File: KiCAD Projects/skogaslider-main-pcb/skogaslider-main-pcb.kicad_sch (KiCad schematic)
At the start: 173 parts, among them J1 USB_C_Receptacle_USB2.0, J2 USB_C_Receptacle_USB2.0, J4 Conn_02x16_Top_Bottom, J5 USB_C_Receptacle_USB2.0, J6 USB_C_Receptacle_USB2.0, Q1 BSS138, U1 NCP1117-3.3_SOT223, U2 MPR121QR2, U3 MPR121QR2, U4 USBLC6-2P6, U5 RP2040, U6 M24C02-RMN, U7 W25Q128JVS, U8 MPR121QR2, Y1 ABLS-12.000MHZ-B4-T

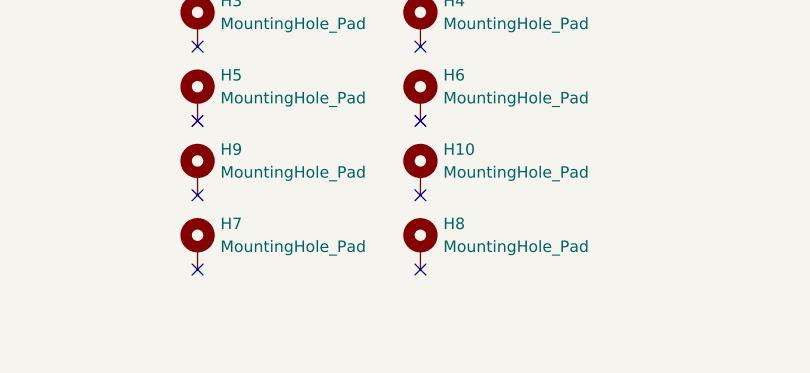
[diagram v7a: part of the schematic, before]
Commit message: Minor revision of the slider PCB to re-arrange the mounting holes to fit the CAD better.
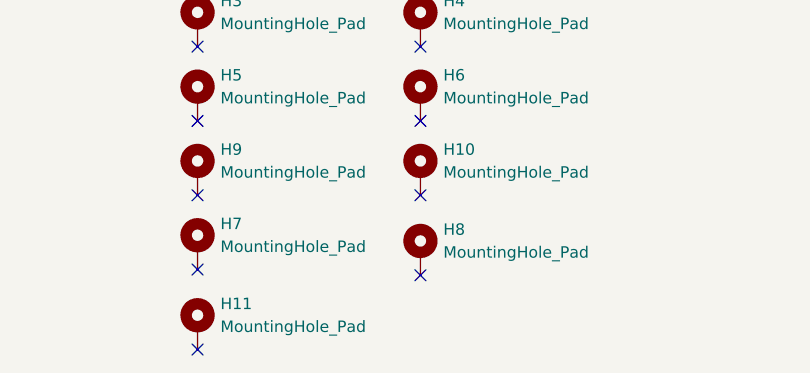
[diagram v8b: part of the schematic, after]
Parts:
- added H11: MountingHole_Pad, MountingHole:MountingHole_3.2mm_M3_DIN965_Pad_TopBottom, symbol Mechanical:MountingHole_Pad
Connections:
- no-connect marks 53 -> 54
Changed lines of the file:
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@@
   (no_connect (at 287.02 128.905))
   (no_connect (at 287.02 131.445))
-  (no_connect (at 133.985 341.63))
+  (no_connect (at 109.22 350.52))
   (no_connect (at 487.045 63.5))
   (no_connect (at 133.985 308.61))
@@
   (no_connect (at 287.02 106.045))
   (no_connect (at 134.62 56.515))
+  (no_connect (at 133.985 342.265))
   (no_connect (at 109.22 308.61))
   (no_connect (at 287.02 108.585))
@@
     (pin "D1")
   )
-  (symbol (lib_id "Mechanical:MountingHole_Pad") (at 133.985 339.09 0) (unit 1)
-    (in_bom yes) (on_board yes) (fields_autoplaced)
-    (property "Reference" "H8" (id 0) (at 136.525 336.5499 0)
-      (effects (font (size 1.27 1.27)) (justify left))
-    )
-    (property "Value" "MountingHole_Pad" (id 1) (at 136.525 339.0899 0)
-      (effects (font (size 1.27 1.27)) (justify left))
-    )
-    (property "Footprint" "MountingHole:MountingHole_3.2mm_M3_DIN965_Pad_TopBottom" (id 2) (at 133.985 339.09 0)
-      (effects (font (size 1.27 1.27)) hide)
-    )
-    (property "Datasheet" "~" (id 3) (at 133.985 339.09 0)
-      (effects (font (size 1.27 1.27)) hide)
-    )
-    (pin "1")
-  )
   (symbol (lib_id "Device:C") (at 454.66 213.36 0) (unit 1)
     (in_bom yes) (on_board yes)
@@
     (pin "2")
   )
+  (symbol (lib_id "Mechanical:MountingHole_Pad") (at 133.985 339.725 0) (unit 1)
+    (in_bom yes) (on_board yes) (fields_autoplaced)
+    (property "Reference" "H8" (id 0) (at 136.525 337.1849 0)
+      (effects (font (size 1.27 1.27)) (justify left))
+    )
+    (property "Value" "MountingHole_Pad" (id 1) (at 136.525 339.7249 0)
+      (effects (font (size 1.27 1.27)) (justify left))
+    )
+    (property "Footprint" "MountingHole:MountingHole_3.2mm_M3_DIN965_Pad_TopBottom" (id 2) (at 133.985 339.725 0)
+      (effects (font (size 1.27 1.27)) hide)
+    )
+    (property "Datasheet" "~" (id 3) (at 133.985 339.725 0)
+      (effects (font (size 1.27 1.27)) hide)
+    )
+    (pin "1")
+  )
   (symbol (lib_id "power:GND") (at 22.225 88.265 0) (unit 1)
     (in_bom yes) (on_board yes)
@@
     (pin "1")
   )
+  (symbol (lib_id "Mechanical:MountingHole_Pad") (at 109.22 347.98 0) (unit 1)
+    (in_bom yes) (on_board yes) (fields_autoplaced)
+    (property "Reference" "H11" (id 0) (at 111.76 345.4399 0)
+      (effects (font (size 1.27 1.27)) (justify left))
+    )
+    (property "Value" "MountingHole_Pad" (id 1) (at 111.76 347.9799 0)
+      (effects (font (size 1.27 1.27)) (justify left))
+    )
+    (property "Footprint" "MountingHole:MountingHole_3.2mm_M3_DIN965_Pad_TopBottom" (id 2) (at 109.22 347.98 0)
+      (effects (font (size 1.27 1.27)) hide)
+    )
+    (property "Datasheet" "~" (id 3) (at 109.22 347.98 0)
+      (effects (font (size 1.27 1.27)) hide)
+    )
+    (pin "1")
+  )
   (symbol (lib_id "Device:C") (at 280.67 55.245 0) (unit 1)
     (in_bom yes) (on_board yes)
@@
       (reference "H7") (unit 1) (value "MountingHole_Pad") (footprint "MountingHole:MountingHole_3.2mm_M3_DIN965_Pad_TopBottom")
     )
-    (path "/854adfe9-458e-47c7-9ed2-06ed6d88edbc"
+    (path "/c47a5136-0069-4f82-a1f5-b27143dad6b2"
       (reference "H8") (unit 1) (value "MountingHole_Pad") (footprint "MountingHole:MountingHole_3.2mm_M3_DIN965_Pad_TopBottom")
     )
@@
       (reference "H10") (unit 1) (value "MountingHole_Pad") (footprint "MountingHole:MountingHole_3.2mm_M3_DIN965_Pad_TopBottom")
     )
+    (path "/eb503603-1f69-4f2a-9451-62f7fe6b23d0"
+      (reference "H11") (unit 1) (value "MountingHole_Pad") (footprint "MountingHole:MountingHole_3.2mm_M3_DIN965_Pad_TopBottom")
+    )
     (path "/def94578-b40c-49d4-b021-539bbd6e35c9"
